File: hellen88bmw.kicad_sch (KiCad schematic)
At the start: 305 parts, among them J1 920-462A2021Y10101, J14 VRIN1, J15 VRIN2, J16 VROUT1, J17 XH-8A, J18 PJ-3250-5A, J19 MiniFit, J2 DNP, J20 ETB, J21 ETB, J3 Conn_01x06, J4 Conn_01x05, J5 Conn_01x12, J6 Conn_01x12, J7 Conn_01x12, J8 Conn_01x12, J9 Conn_01x12, M1 Module-power12-0.2, M10 Module-ign8-0.1, M11 Module-mcu144-0.5, M12 Module-knock-0.1, M13 Module-sd-0.1, M2 Module-can-0.1, M3 Module-wbo-0.2, M4 Module-can-0.1, M5 Module-power5-0.2, M6 Module-vr-0.1, M7 Module-input-0.1, M8 Module-knock-0.1, M9 Module-output-0.2, P1 P, P15 Pad, P16 Pad, P17 Pad, P18 Pad, P19 Pad, P2 P, P21 Pad, P22 Pad, P23 Pad, P24 Pad, P25 Pad, P26 Pad, P27 Pad, P28 Pad, P29 Pad, P3 P, P30 Pad, P31 Pad, P32 Pad, P4 P, P5 P, P6 P, Q1 NGD8201AN, Q10 AUIPS2041L, Q2 NGD8201AN, Q3 NGD8201AN, Q4 NGD8201AN, Q5 NGD8201AN, Q6 NGD8201AN, Q7 NGD8201AN, Q8 NGD8201AN, Q9 AUIPS2041L, SW1 RESET, SW2 RESET, U1 MPXA6115A, U2 MPX4_MAP, U3 LIS2DW12TR, U4 LPS25HB, U5 MCP6002-xSN, U6 L6205PD

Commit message: PCB refactoring started
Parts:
- removed J18: PJ-3250-5A, Connector_Audio:Jack_3.5mm_CUI_SJ1-3535NG_Horizontal, symbol Connector:AudioJack3_Switch
- removed P15, P16, P17, P18, P19, P21, P22, P23, P24, P25, P26, P27, P28, P29, P30, P31, P32: Pad, hellen-one-common:PAD-TH, symbol hellen-one-common:Pad
- added J18: AudioJack_THR, hellen-one-common:Jack_3.5mm_PJ-3250-5A, symbol hellen-one-common:AudioJack_THR
- added VIN2, VIN3, VIN4, VIN5, VIN6: VIN8, Connector_PinHeader_1.00mm:PinHeader_1x01_P1.00mm_Vertical, symbol Connector_Generic:Conn_01x01
- added VOUT12, VOUT13, VOUT16, VOUT17, VOUT18, VOUT19, VOUT20, VOUT21, VOUT24, VOUT25, VOUT26, VOUT27: VOUT4, Connector_PinHeader_1.00mm:PinHeader_1x01_P1.00mm_Vertical, symbol Connector_Generic:Conn_01x01
- G1, G4: footprint footprints:LOGO -> hellen-one-common:LOGO
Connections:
- net GND: now also J18.S
- net at M9.W35 (LOW11): now also VOUT16.1 (Pin_1)
- net at M7.S22 (IN_RES3): now also VIN4.1 (Pin_1)
- net at M9.W21 (LOW1): now also VOUT24.1 (Pin_1)
- net at M9.W37 (LOW8_HIGH2): now also VOUT12.1 (Pin_1)
- net at M9.W25 (LOW6_DIODE): now also VOUT26.1 (Pin_1)
- net at M7.S23 (IN_RES1): now also VIN2.1 (Pin_1)
- net at M7.S25 (IN_O2S2): now also VIN6.1 (Pin_1)
- net at M7.S26 (IN_RES2): now also VIN3.1 (Pin_1)
- net at M7.S9 (IN_O2S): now also VIN5.1 (Pin_1)
- net at M9.W33 (SOLENOID_A1): now also VOUT18.1 (Pin_1)
- net at C8.2: now also J18.R
- net at C7.2: now also J18.T
- net at M9.W29 (LOW2): now also VOUT25.1 (Pin_1)
- net at M9.W39 (LOW7_HIGH1): now also VOUT27.1 (Pin_1)
- net at M9.W27 (LOW9): now also VOUT13.1 (Pin_1)
- net at M9.W30 (SOLENOID_B2): now also VOUT21.1 (Pin_1)
- net at M9.W31 (SOLENOID_B1): now also VOUT20.1 (Pin_1)
- net at M9.W32 (SOLENOID_A2): now also VOUT19.1 (Pin_1)
- net at M9.W36 (LOW12): now also VOUT17.1 (Pin_1)
- no-connect marks 105 -> 104

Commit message: Upd pcb
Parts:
- removed J3: Conn_01x06, Connector_PinHeader_2.54mm:PinHeader_1x06_P2.54mm_Vertical, symbol Connector_Generic:Conn_01x06
- removed R17, R18, R19, R20, R21, R22, R23, R24: 0, Resistor_SMD:R_0402_1005Metric, symbol Device:R
- added R17, R18, R19, R20, R21, R22, R23, R24: 22, hellen-one-common:R0603, symbol hellen-one-common:Res
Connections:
- net GNDA is gone; now on net GND: M7.J11 (PULL_RES3), M7.J12 (PULL_MAP3), M7.J13 (PULL_MAP2), M7.J14 (PULL_MAP1), M7.J19 (PULL_TPS), M7.J2 (PULL_GNDA), M7.J20 (PULL_O2S), M7.J22 (PULL_KNOCK), M7.J23 (PULL_SENS4), M7.J25 (PULL_SENS2), M7.J26 (PULL_SENS1), M7.J3 (PULL_RES2), M7.J4 (PULL_O2S2), M7.J5 (PULL_PPS), M7.J6 (PULL_RES1), M7.N2 (GNDA), R16.1, R25.1, R26.1, R35.1, R4.1
- net +12V: no longer D10.1 (K), D3.1 (K), D44.1 (K), D8.1 (K), R15.1, RN7.1 (R1.1), RN7.2 (R2.1), RN7.3 (R3.1), RN7.4 (R4.1), RN8.1 (R1.1), RN8.2 (R2.1), RN8.3 (R3.1), RN8.4 (R4.1)
- net +12V_RAW: now also D10.1 (K), D3.1 (K), D44.1 (K), D8.1 (K), R15.1
- net +5V: now also J4.4 (Pin_4)
- net +5VA: no longer J4.4 (Pin_4)
- net OUT_IGN1: now also R17.2
- net OUT_IGN2: now also R21.2
- net OUT_IGN3: now also R20.2
- net OUT_IGN4: now also R19.2
- net OUT_IGN5: now also R18.2
- net OUT_IGN6: now also R22.2
- net OUT_IGN7: now also R23.2
- net OUT_IGN8: now also R24.2
- net HV_7: now reaches F1.1, PP1.22
- net HV_4: now reaches F2.1, PP1.23
- net HV_6: now reaches F3.1, PP1.24
- net HV_5: now reaches F4.1, PP1.25
- net HV_8: now reaches F5.1, PP1.49
- net HV_1: now reaches F6.1, PP1.50
- net HV_2: now reaches F7.1, PP1.51
- net HV_3: now reaches F8.1, PP1.52
- net at Q6.1 (G): now also R18.1
- net at Q5.1 (G): now also R20.1
- net at Q4.1 (G): now also R22.1
- net at Q1.1 (G): now also R17.1
- net at Q2.1 (G): now also R19.1
- net at Q3.1 (G): now also R21.1
- net at Q7.1 (G): now also R23.1
- net at Q8.1 (G): now also R24.1
- net 12V_prot: now reaches M9.W5 (V12P), VOUT6.1 (Pin_1)
- net 12V_prot: now also RN7.1 (R1.1), RN7.2 (R2.1), RN7.3 (R3.1), RN7.4 (R4.1), RN8.1 (R1.1), RN8.2 (R2.1), RN8.3 (R3.1), RN8.4 (R4.1)
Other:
- moved on the sheet: F1, F2, F3, F4, F5, F6, F7, F8, VOUT6

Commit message: DRC fix, test export
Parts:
- removed G1, G4: Conn_01x01, hellen-one-common:LOGO, symbol Connector_Generic:Conn_01x01
- removed G2, G3: Conn_01x01, rusefi_lib:LOGO, symbol Connector_Generic:Conn_01x01
- removed J2: DNP, Connector_PinHeader_2.00mm:PinHeader_1x05_P2.00mm_Vertical, symbol hellen-one-common:USB_B_Mini
- removed J5, J6, J7, J8, J9: Conn_01x12, Connector_PinHeader_2.54mm:PinHeader_1x12_P2.54mm_Vertical, symbol Connector_Generic:Conn_01x12
- removed JP20, JP21: DNP, rusefi_lib:SM0805_jumper, symbol Jumper:Jumper_2_Open
- removed U6: L6205PD, kicad6:SO20POWER, symbol L6205PD:L6205PD
- added BT1: BATTERY_CR2032, Battery:BatteryHolder_Keystone_1060_1x2032, symbol art-electro-power:BATTERY_CR2032
- added D9: 1N4148WS, hellen-one-common:SOD-323, symbol hellen-one-common:1N4148WS
- added G1: LOGO, hellen-one-common:LOGO, symbol hellen-one-common:LOGO
- added G2: LOGO, rusefi_lib:LOGO, symbol logo:LOGO
- added G3, G4, G6, G7: PROTO_AREA, hellen-one-common:PROTO_AREA, symbol hellen-one-common:PROTO_AREA
- added J2: Conn_01x05, Connector_PinHeader_2.00mm:PinHeader_1x05_P2.00mm_Vertical, symbol Connector_Generic:Conn_01x05
- added JP20, JP21: Jumper_2_Open, hellen-one-common:PAD-0805-PAD, symbol hellen-one-common:Jumper-Pad-Pad
- added U6: L6205PD, hellen-one-common:SO20POWER, symbol hellen-one-common:L6205PD
- J1: value 920-462A2021Y10101 -> USB_B_Mini; footprint rusefi_lib_private:USB-MINI-B-VERTICAL -> hellen-one-common:USB-MINI-B-VERTICAL
- JP1, JP14, JP16, JP17, JP2, JP26, JP27, JP29, JP3, JP31, JP32, JP33, JP35, JP36, JP4, JP42, JP43, JP46, JP47, JP48, JP5, JP59, JP7, JP73, JP77, JP78, JP85, JP86: footprint rusefi_lib:SM0805_jumper -> hellen-one-common:PAD-0805-PAD; symbol Jumper:Jumper_2_Open -> hellen-one-common:Jumper-Pad-Pad
- JP41: footprint rusefi_lib:SM0805_jumper -> hellen-one-common:PAD-0805-PAD; symbol Jumper:Jumper_2_Open -> hellen-one-common:Jumper-Pad-Pad; LCSC C17477 -> (none); MyComment (none) -> DNP
- JP54: value DNP -> Jumper_2_Open; footprint rusefi_lib:SM0805_jumper -> hellen-one-common:PAD-1206-PAD; symbol Jumper:Jumper_2_Open -> hellen-one-common:Fuse-Pad-Pad; LCSC DNP -> (none); MyComment (none) -> DNP
- JP56: footprint rusefi_lib:SM0805_jumper -> hellen-one-common:PAD-1206-PAD; symbol Jumper:Jumper_2_Open -> hellen-one-common:Fuse-Pad-Pad; LCSC C17477 -> C182446
- JP6: value DNP -> Jumper_2_Open; footprint rusefi_lib:SM0805_jumper -> hellen-one-common:PAD-0805-PAD; symbol Jumper:Jumper_2_Open -> hellen-one-common:Jumper-Pad-Pad; LCSC DNP -> (none); MyComment (none) -> DNP
- Q10, Q9: value AUIPS2041L -> AUIPS2041LTR
- R5, R6: LCSC NA -> (none)
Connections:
- net +12V_RAW: now also U6.19 (VSB), U6.2 (VSA)
- net +ETB: now also U6.15 (IN2B), U6.7 (IN2A)
- net -ETB: now also U6.14 (IN1B), U6.6 (IN1A)
- net GND: now also BT1.2 (-), J2.5 (Pin_5), U6.1 (GND@1), U6.10 (GND@2), U6.11 (GND@3), U6.13 (SENSEB), U6.20 (GND@4), U6.8 (SENSEA), U6.SLUG1 (SLUG@1), U6.SLUG2 (SLUG@2), U6.SLUG3 (SLUG@3)
- net OUT_ETB+: now also U6.18 (OUT2B), U6.3 (OUT2A)
- net OUT_ETB-: now also U6.12 (OUT1B), U6.9 (OUT1A)
- net USBM: now also J2.2 (Pin_2), JP21.2
- net USBP: now also J2.3 (Pin_3), JP20.2
- net VBAT: now also D9.1 (K)
- net VBUS: now also J2.1 (Pin_1)
- net at PP1.20: now also JP20.1
- net at PP1.21: now also JP21.1
- net at C10.1, R28.1: now also U6.16 (ENB), U6.5 (ENA)
- net at C12.2: now also U6.4 (VCP)
- net at C15.2, D33.1 (K): now also U6.17 (VBOOT)
- new net: BT1.1 (+), D9.2 (A)
- new net: G6.1, G6.11, G6.6
- new net: G6.10, G6.15, G6.5
- new net: G6.12, G6.2, G6.7
- new net: G6.13, G6.3, G6.8
- new net: G6.14, G6.4, G6.9
- new net: G3.1, G3.11, G3.6
- new net: G3.10, G3.15, G3.5
- new net: G3.12, G3.2, G3.7
- new net: G3.13, G3.3, G3.8
- new net: G3.14, G3.4, G3.9
- new net: G4.1, G4.11, G4.6
- new net: G4.10, G4.15, G4.5
- new net: G4.12, G4.2, G4.7
- new net: G4.13, G4.3, G4.8
- new net: G4.14, G4.4, G4.9
- new net: G7.1, G7.11, G7.6
- new net: G7.10, G7.15, G7.5
- new net: G7.12, G7.2, G7.7
- new net: G7.13, G7.3, G7.8
- new net: G7.14, G7.4, G7.9
- no-connect marks 104 -> 39
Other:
- moved on the sheet: C3, SW2

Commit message: Wbo 0.3
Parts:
- removed M3: Module-wbo-0.2, hellen-one-wbo-0.2:wbo, symbol hellen-one-wbo-0.2:Module-wbo-0.2
- added M3: Module-wbo-0.3, hellen-one-wbo-0.3:wbo, symbol hellen-one-wbo-0.3:Module-wbo-0.3
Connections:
- net +5V: now also M3.W1 (V5_IN)
- net GND: now also M3.E6 (LSU_H-), M3.G (GND)
- net LSU_CALIBR_RES: now also M3.E4 (LSU_Rtrim)
- net LSU_HEAT-: now also M3.E5 (LSU_H+)
- net LSU_PUMP_I: now also M3.E3 (LSU_Ip)
- net LSU_SENSOR_U: now also M3.E1 (LSU_Un)
- net LSU_SENSOR_U/PUMP_I: now also M3.E2 (LSU_Vm)
- net at M4.V2 (CAN_VIO): now also M3.W2 (CAN_VIO)
- net at M4.V6 (CAN_RX): now also M3.W3 (CAN_RX)
- net at M4.V5 (CAN_TX): now also M3.W4 (CAN_TX)
- new net: M3.J1 (SEL1), M3.J_GND1 (PULL_DOWN1)
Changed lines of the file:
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@@
     (pin "J9")
   )
-  (symbol (lib_id "hellen-one-wbo-0.2:Module-wbo-0.2") (at 711.2 45.72 0) (mirror y) (unit 1)
-    (in_bom yes) (on_board yes)
-    (property "Reference" "M3" (id 0) (at 694.69 41.6368 0))
-    (property "Value" "Module-wbo-0.2" (id 1) (at 694.69 43.9355 0))
-    (property "Footprint" "hellen-one-wbo-0.2:wbo" (id 2) (at 685.8 44.45 0)
+  (symbol (lib_id "hellen-one-wbo-0.3:Module-wbo-0.3") (at 711.2 45.72 0) (mirror y) (unit 1)
+    (in_bom yes) (on_board yes) (fields_autoplaced)
+    (property "Reference" "M3" (id 0) (at 694.69 41.8804 0))
+    (property "Value" "Module-wbo-0.3" (id 1) (at 694.69 44.6555 0))
+    (property "Footprint" "hellen-one-wbo-0.3:wbo" (id 2) (at 685.8 44.45 0)
       (effects (font (size 1.27 1.27)) hide)
     )
@@
       (reference "M2") (unit 1) (value "Module-can-0.1") (footprint "hellen-one-can-0.1:can")
     )
-    (path "/c145cecf-e6fb-4f01-91ef-f3fbeb476d3a"
-      (reference "M3") (unit 1) (value "Module-wbo-0.2") (footprint "hellen-one-wbo-0.2:wbo")
+    (path "/8f102ce2-a7ee-4380-a4d7-2d832c7c5a10"
+      (reference "M3") (unit 1) (value "Module-wbo-0.3") (footprint "hellen-one-wbo-0.3:wbo")
     )
     (path "/e3bc811d-dd8e-4541-8083-b187fedfc7e2"

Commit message: Fresh export. JLC adjustments
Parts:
- removed SW1, SW2: RESET, Button_Switch_SMD:SW_SPST_B3U-1000P-B, symbol Switch:SW_SPST
- added SW1, SW2: Button_SPST, hellen-one-common:SMD-2_2.9x3.9x1.7, symbol hellen-one-common:Button_SPST
- C12: LCSC C541443 -> C15195
- J20: LCSC C343639 -> (none)
- J21: value ETB -> PPS; LCSC C343639 -> (none)
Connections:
- net +3V3: now also SW1.2
- net BOOT0: now also SW1.1
- net GND: now also SW2.2
- net NRESET: now also SW2.1
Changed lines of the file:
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@@
   (junction (at 641.35 60.96) (diameter 0.9144) (color 0 0 0 0))
   (junction (at 641.35 63.5) (diameter 0.9144) (color 0 0 0 0))
-  (junction (at 693.42 265.43) (diameter 0.9144) (color 0 0 0 0))
+  (junction (at 693.42 265.43) (diameter 0) (color 0 0 0 0))
   (junction (at 701.04 187.96) (diameter 0.9144) (color 0 0 0 0))
   (junction (at 703.58 120.65) (diameter 1.016) (color 0 0 0 0))
@@
     (stroke (width 0) (type solid) (color 0 0 0 0))
   )
-  (wire (pts (xy 637.54 267.97) (xy 650.24 267.97))
+  (wire (pts (xy 637.54 267.97) (xy 647.7 267.97))
     (stroke (width 0) (type solid) (color 0 0 0 0))
   )
@@
     (stroke (width 0) (type solid) (color 0 0 0 0))
   )
-  (wire (pts (xy 662.94 267.97) (xy 660.4 267.97))
-    (stroke (width 0) (type solid) (color 0 0 0 0))
-  )
   (wire (pts (xy 665.48 66.04) (xy 665.48 67.31))
     (stroke (width 0) (type solid) (color 0 0 0 0))
@@
     (stroke (width 0) (type solid) (color 0 0 0 0))
   )
-  (wire (pts (xy 693.42 265.43) (xy 695.96 265.43))
-    (stroke (width 0) (type solid) (color 0 0 0 0))
-  )
   (wire (pts (xy 693.42 275.59) (xy 693.42 276.86))
     (stroke (width 0) (type solid) (color 0 0 0 0))
@@
     (stroke (width 0) (type solid) (color 0 0 0 0))
   )
-  (wire (pts (xy 706.12 265.43) (xy 708.66 265.43))
-    (stroke (width 0) (type solid) (color 0 0 0 0))
-  )
   (wire (pts (xy 711.2 187.96) (xy 711.2 190.5))
     (stroke (width 0) (type solid) (color 0 0 0 0))
@@
     (pin "2")
   )
-  (symbol (lib_id "Switch:SW_SPST") (at 655.32 267.97 0) (unit 1)
-    (in_bom yes) (on_board yes)
-    (property "Reference" "SW1" (id 0) (at 650.24 266.7 0))
-    (property "Value" "RESET" (id 1) (at 655.32 264.16 0)
-      (effects (font (size 1.27 1.27)) hide)
-    )
-    (property "Footprint" "Button_Switch_SMD:SW_SPST_B3U-1000P-B" (id 2) (at 655.32 267.97 0)
-      (effects (font (size 1.27 1.27)) hide)
-    )
-    (property "Datasheet" "~" (id 3) (at 655.32 267.97 0)
-      (effects (font (size 1.27 1.27)) hide)
-    )
-    (property "LCSC" "	C231329" (id 4) (at 655.32 267.97 0)
-      (effects (font (size 1.27 1.27)) hide)
-    )
-    (property "Comment" "" (id 5) (at 655.32 267.97 0)
-      (effects (font (size 1.27 1.27)) hide)
-    )
-    (pin "1")
-    (pin "2")
-  )
-  (symbol (lib_id "Switch:SW_SPST") (at 701.04 265.43 0) (unit 1)
-    (in_bom yes) (on_board yes)
-    (property "Reference" "SW2" (id 0) (at 701.04 262.636 0))
-    (property "Value" "RESET" (id 1) (at 701.04 261.62 0)
-      (effects (font (size 1.27 1.27)) hide)
-    )
-    (property "Footprint" "Button_Switch_SMD:SW_SPST_B3U-1000P-B" (id 2) (at 701.04 265.43 0)
-      (effects (font (size 1.27 1.27)) hide)
-    )
-    (property "Datasheet" "~" (id 3) (at 701.04 265.43 0)
-      (effects (font (size 1.27 1.27)) hide)
-    )
-    (property "LCSC" "	C231329" (id 4) (at 701.04 265.43 0)
-      (effects (font (size 1.27 1.27)) hide)
-    )
-    (pin "1")
-    (pin "2")
-  )
   (symbol (lib_id "hellen-one-common:Jumper-Pad-Pad") (at 71.12 86.36 0) (mirror x) (unit 1)
     (in_bom yes) (on_board yes)
@@
       (effects (font (size 1.27 1.27)) hide)
     )
-    (property "LCSC" "C541443" (id 4) (at 207.01 422.91 0)
+    (property "LCSC" "C15195" (id 4) (at 207.01 422.91 0)
       (effects (font (size 1.27 1.27)) hide)
     )
@@
     )
   )
+  (symbol (lib_id "hellen-one-common:Button_SPST") (at 652.78 265.43 0) (unit 1)
+    (in_bom yes) (on_board yes)
+    (property "Reference" "SW1" (id 0) (at 650.24 266.7 0))
+    (property "Value" "Button_SPST" (id 1) (at 652.78 269.24 0))
+    (property "Footprint" "hellen-one-common:SMD-2_2.9x3.9x1.7" (id 2) (at 652.78 265.43 0)
+      (effects (font (size 1.27 1.27)) hide)
+    )
+    (property "Datasheet" "" (id 3) (at 652.78 265.43 0)
+      (effects (font (size 1.27 1.27)) hide)
+    )
+    (property "LCSC" "C115357" (id 4) (at 652.78 265.43 0)
+      (effects (font (size 1.27 1.27)) hide)
+    )
+    (pin "1")
+    (pin "2")
+  )
+  (symbol (lib_id "hellen-one-common:Button_SPST") (at 698.5 262.89 0) (unit 1)
+    (in_bom yes) (on_board yes)
+    (property "Reference" "SW2" (id 0) (at 697.23 264.16 0))
+    (property "Value" "Button_SPST" (id 1) (at 701.04 266.7 0))
+    (property "Footprint" "hellen-one-common:SMD-2_2.9x3.9x1.7" (id 2) (at 698.5 262.89 0)
+      (effects (font (size 1.27 1.27)) hide)
+    )
+    (property "Datasheet" "" (id 3) (at 698.5 262.89 0)
+      (effects (font (size 1.27 1.27)) hide)
+    )
+    (property "LCSC" "C115357" (id 4) (at 698.5 262.89 0)
+      (effects (font (size 1.27 1.27)) hide)
+    )
+    (pin "1")
+    (pin "2")
+  )
   (symbol (lib_id "Connector_Generic:Conn_01x04") (at 367.03 292.1 0) (unit 1)
     (in_bom yes) (on_board yes) (fields_autoplaced)
@@
       (effects (font (size 1.27 1.27)) (justify left))
     )
-    (property "Value" "ETB" (id 1) (at 369.57 294.64 0)
+    (property "Value" "PPS" (id 1) (at 369.57 294.64 0)
       (effects (font (size 1.27 1.27)) (justify left))
     )
@@
       (effects (font (size 1.27 1.27)) hide)
     )
-    (property "LCSC" "C343639" (id 4) (at 367.03 292.1 0)
-      (effects (font (size 1.27 1.27)) hide)
-    )
     (pin "1")
     (pin "2")
@@
       (effects (font (size 1.27 1.27)) hide)
     )
-    (property "LCSC" "C343639" (id 4) (at 345.44 289.56 0)
-      (effects (font (size 1.27 1.27)) hide)
-    )
     (pin "1")
     (pin "2")
@@
     )
     (path "/ce96e045-4eec-49f9-87cd-8ae99dfc13c8"
-      (reference "J21") (unit 1) (value "ETB") (footprint "Connector_PinHeader_2.54mm:PinHeader_1x04_P2.54mm_Vertical")
+      (reference "J21") (unit 1) (value "PPS") (footprint "Connector_PinHeader_2.54mm:PinHeader_1x04_P2.54mm_Vertical")
     )
     (path "/00000000-0000-0000-0000-00005f7c5b0c"
@@
       (reference "RN8") (unit 1) (value "4.7k") (footprint "Resistor_SMD:R_Array_Concave_4x0603")
     )
-    (path "/6b6d9cce-9449-465a-86d0-676d54a1bd13"
-      (reference "SW1") (unit 1) (value "RESET") (footprint "Button_Switch_SMD:SW_SPST_B3U-1000P-B")
+    (path "/ad8ca391-84c6-4f21-b8ec-c88539aca194"
+      (reference "SW1") (unit 1) (value "Button_SPST") (footprint "hellen-one-common:SMD-2_2.9x3.9x1.7")
     )
-    (path "/c7277d80-f3af-46ed-b785-f515ad596404"
-      (reference "SW2") (unit 1) (value "RESET") (footprint "Button_Switch_SMD:SW_SPST_B3U-1000P-B")
+    (path "/967a19d5-b945-4a74-aa9d-0b0f89f1d2fc"
+      (reference "SW2") (unit 1) (value "Button_SPST") (footprint "hellen-one-common:SMD-2_2.9x3.9x1.7")
     )
     (path "/332a6032-cc5f-4729-86b9-d7b8103a40de"

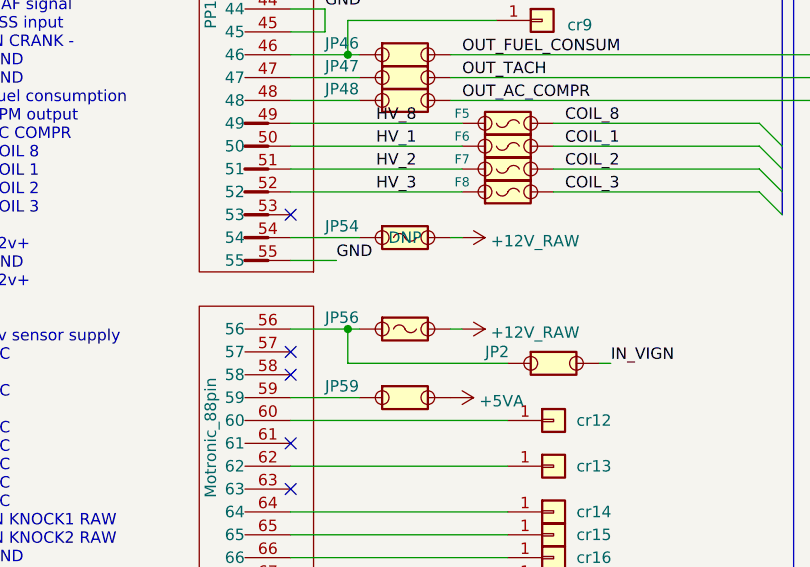
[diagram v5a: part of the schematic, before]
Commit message: VIGN fix
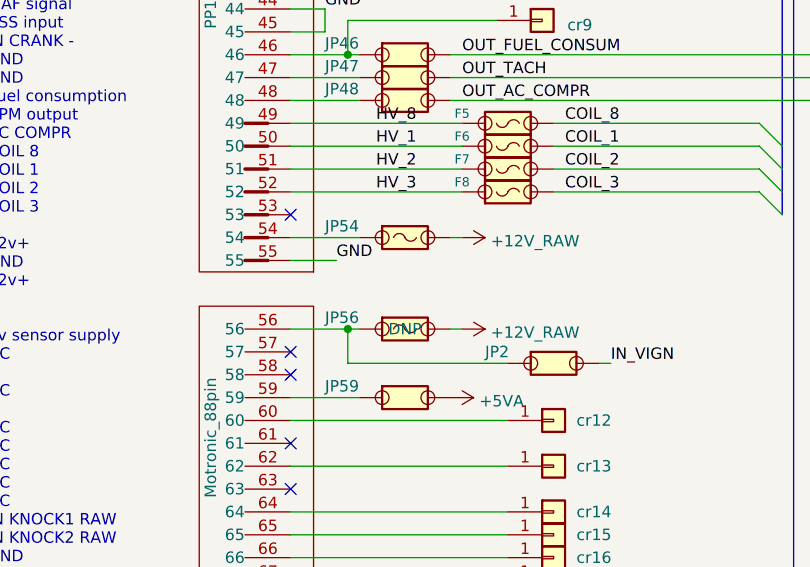
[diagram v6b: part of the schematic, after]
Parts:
- JP54: LCSC (none) -> C182446; MyComment DNP -> (none)
- JP56: LCSC C182446 -> (none); MyCooment (none) -> DNP
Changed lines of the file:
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@@
       (effects (font (size 1.524 1.524)) hide)
     )
-    (property "MyComment" "DNP" (id 5) (at 71.12 227.33 0))
+    (property "MyComment" "" (id 5) (at 71.12 227.33 0))
+    (property "LCSC" "C182446" (id 6) (at 71.12 227.33 0)
+      (effects (font (size 1.27 1.27)) hide)
+    )
     (pin "1")
     (pin "2")
@@
       (effects (font (size 1.524 1.524)) hide)
     )
-    (property "LCSC" "C182446" (id 4) (at 71.12 233.68 0)
-      (effects (font (size 1.27 1.27)) hide)
-    )
+    (property "MyCooment" "DNP" (id 5) (at 71.12 237.49 0))
     (pin "1")
     (pin "2")
